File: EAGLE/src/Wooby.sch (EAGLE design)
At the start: 14 parts, among them J1 TB001-500-04BE, J2 TB001-500-04BE, J3 TB001-500-04BE, U1 GY-521MPU6050

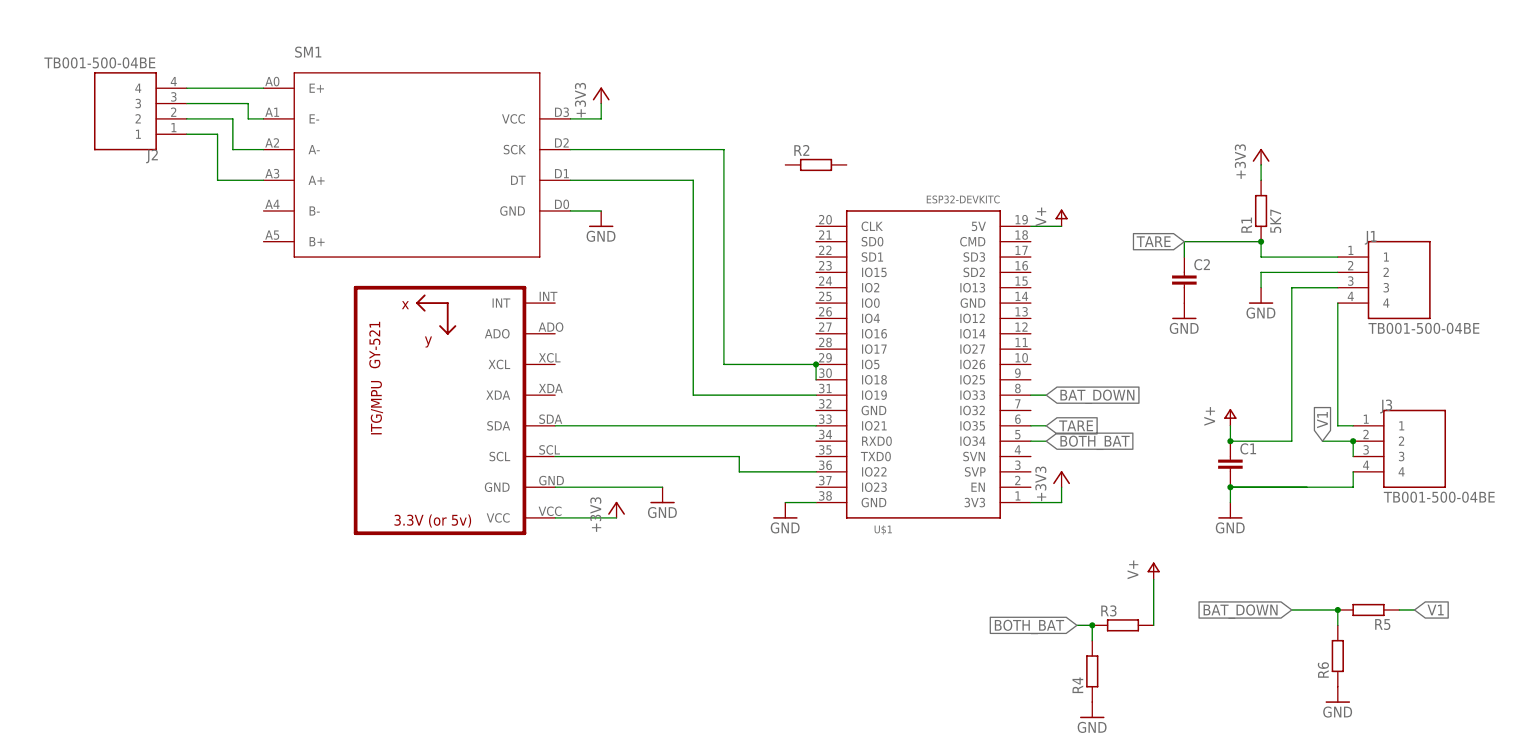
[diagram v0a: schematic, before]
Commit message: [PCB] Size 106mm x 40mm with terminal blocks 5mm, 2 pins.
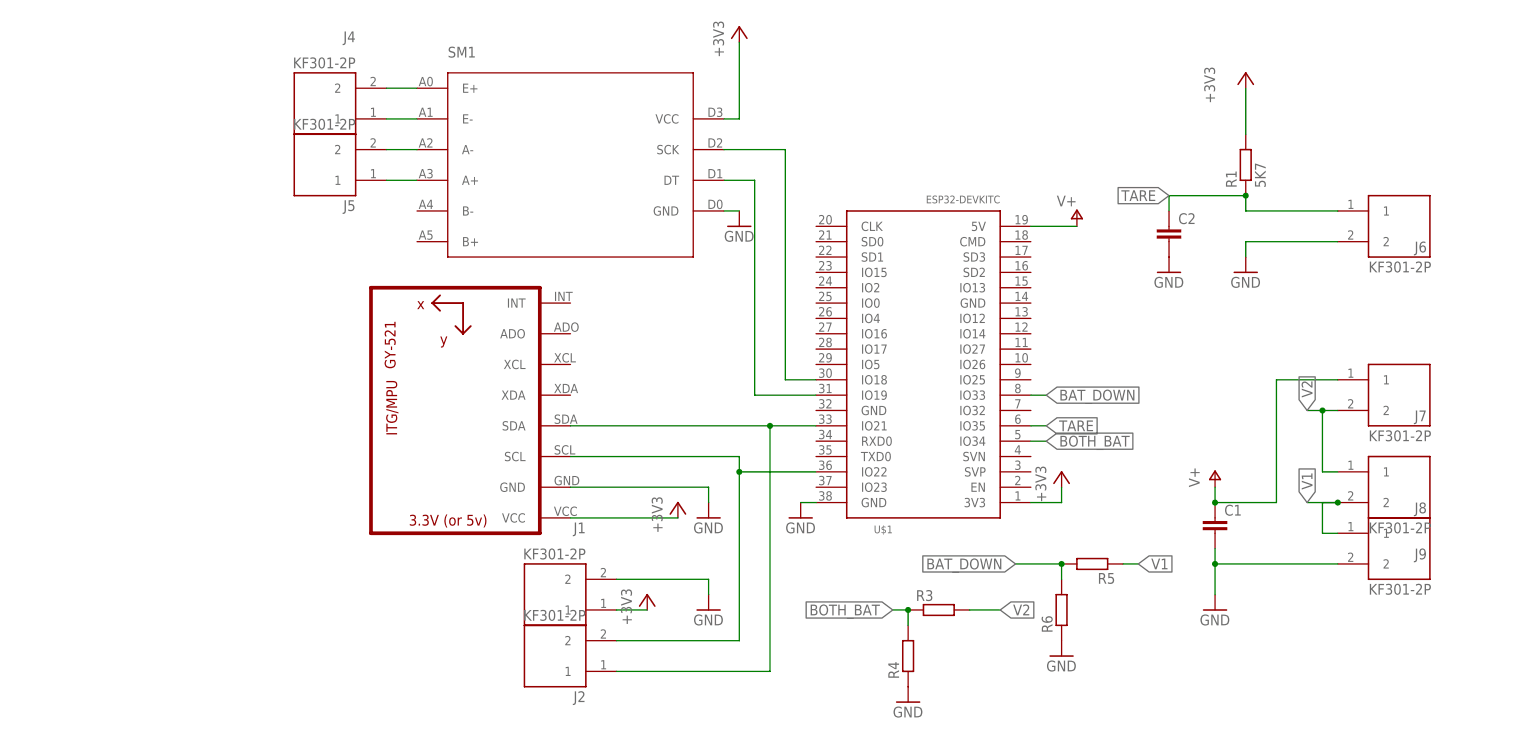
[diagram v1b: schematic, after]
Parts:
- removed J3: TB001-500-04BE, TB001-500-04BE:TB001-500-04BE
- removed R2: (no value), rcl:R-EU_0207/10
- added J4, J5, J6, J7, J8, J9: KF301-2P, KF301-2P:KF301-2P
- J1, J2: value TB001-500-04BE -> KF301-2P; device TB001-500-04BE:TB001-500-04BE -> KF301-2P:KF301-2P
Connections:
- removed net N$1: J1.4, J3.1
- new net V2: J7.2, J8.1, R3.2
- net +3V3: now also J1.1
- net GND: now also J6.2, J9.2; no longer J3.4
- net N$10: no longer U$1.IO5
- net N$2: now also J4.2; no longer J2.4
- net N$3: now also J4.1; no longer J2.3
- net N$4: now also J5.2; no longer J2.2
- net N$5: now also J5.1; no longer J2.1
- net N$6: now also J2.2
- net N$7: now also J2.1
- net TARE: now also J6.1; no longer J1.1
- net V+: now also J7.1; no longer J1.3, R3.2
- net V1: now also J8.2, J9.1; no longer J3.2, J3.3
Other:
- moved on the sheet: C1, C2, R1, R3, R4, R5, R6, SM1

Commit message: [PCB] Version 1
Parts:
- removed J1, J4, J6, J7, J8, J9: KF301-2P, KF301-2P:KF301-2P
- added BAT_BOT, BAT_TOP, CELL, LCD, ON_BTN, TARE: 691210910002, 691210910002:691210910002
- J2, J5: value KF301-2P -> 691210910002; device KF301-2P:KF301-2P -> 691210910002:691210910002
- renumbered U$1 to ESP32-DEVKITC
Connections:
- removed net N$3 (its old number): J4.1, SM1.E-
- new net N$1: CELL.1, SM1.E-
- net +3V3: now also LCD.1; no longer J1.1
- net BAT_DOWN: now also ESP32-DEVKITC.BAT_BOT; no longer ESP32-DEVKITC.IO33
- net BOTH_BAT: now also ESP32-DEVKITC.BATS; no longer ESP32-DEVKITC.IO34
- net GND: now also BAT_BOT.2, LCD.2, TARE.2; no longer J1.2, J6.2, J9.2
- net N$10: now also ESP32-DEVKITC.SCK; no longer ESP32-DEVKITC.IO18
- net N$2: now also CELL.2; no longer J4.2
- net N$6: now also ESP32-DEVKITC.SCL; no longer ESP32-DEVKITC.IO22
- net N$7: now also ESP32-DEVKITC.SDA; no longer ESP32-DEVKITC.IO21
- net TARE: now also ESP32-DEVKITC.TARE, TARE.1; no longer ESP32-DEVKITC.IO35, J6.1
- net V+: now also ON_BTN.1; no longer J7.1
- net V1: now also BAT_BOT.1, BAT_TOP.2; no longer J8.2, J9.1
- net V2: now also BAT_TOP.1, ON_BTN.2; no longer J7.2, J8.1

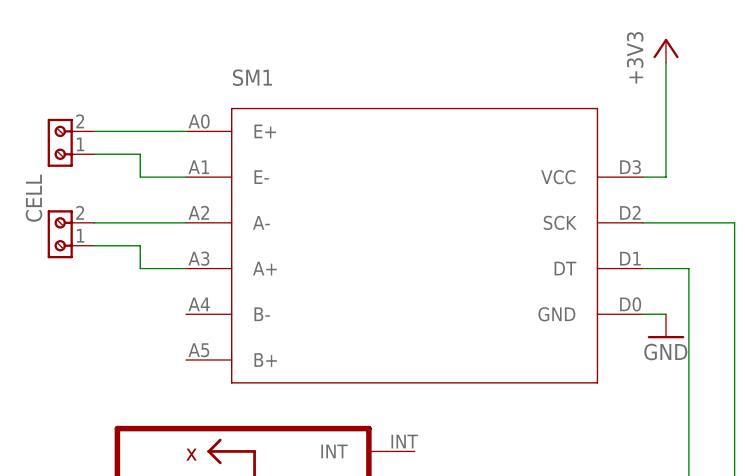
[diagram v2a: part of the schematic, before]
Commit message: Changes on several folders
EAGLE:
Small change to name the inputs of the HX711
ESP32:
Update with latest code with Bluetooth (not working). A cleaning will be done to make it work.
Python:
Latest code with the library and new datasets.
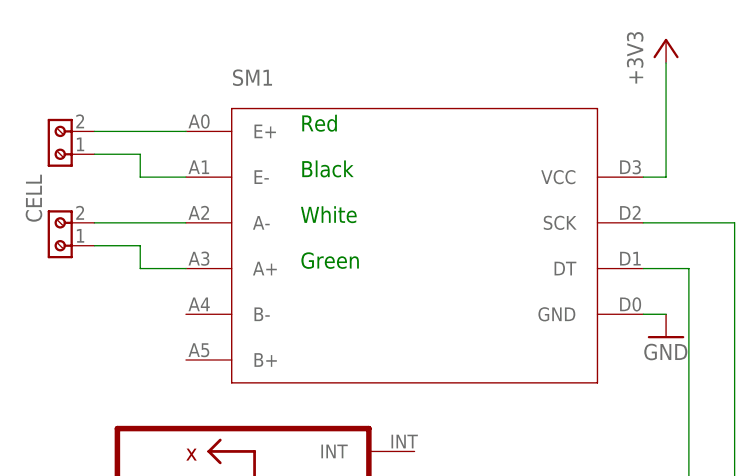
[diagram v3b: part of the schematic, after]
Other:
- note added: "Black"
- note added: "Green"
- note added: "Red"
- note added: "White"
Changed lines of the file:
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@@
 <?xml version="1.0" encoding="utf-8"?>
 <!DOCTYPE eagle SYSTEM "eagle.dtd">
-<eagle version="9.6.1">
+<eagle version="9.6.2">
 <drawing>
 <settings>
@@
 <sheet>
 <plain>
+<text x="2.54" y="68.58" size="1.778" layer="91">Green</text>
+<text x="2.54" y="78.74" size="1.778" layer="91">Black</text>
+<text x="2.54" y="73.66" size="1.778" layer="91">White</text>
+<text x="2.54" y="83.82" size="1.778" layer="91">Red</text>
 </plain>
 <instances>

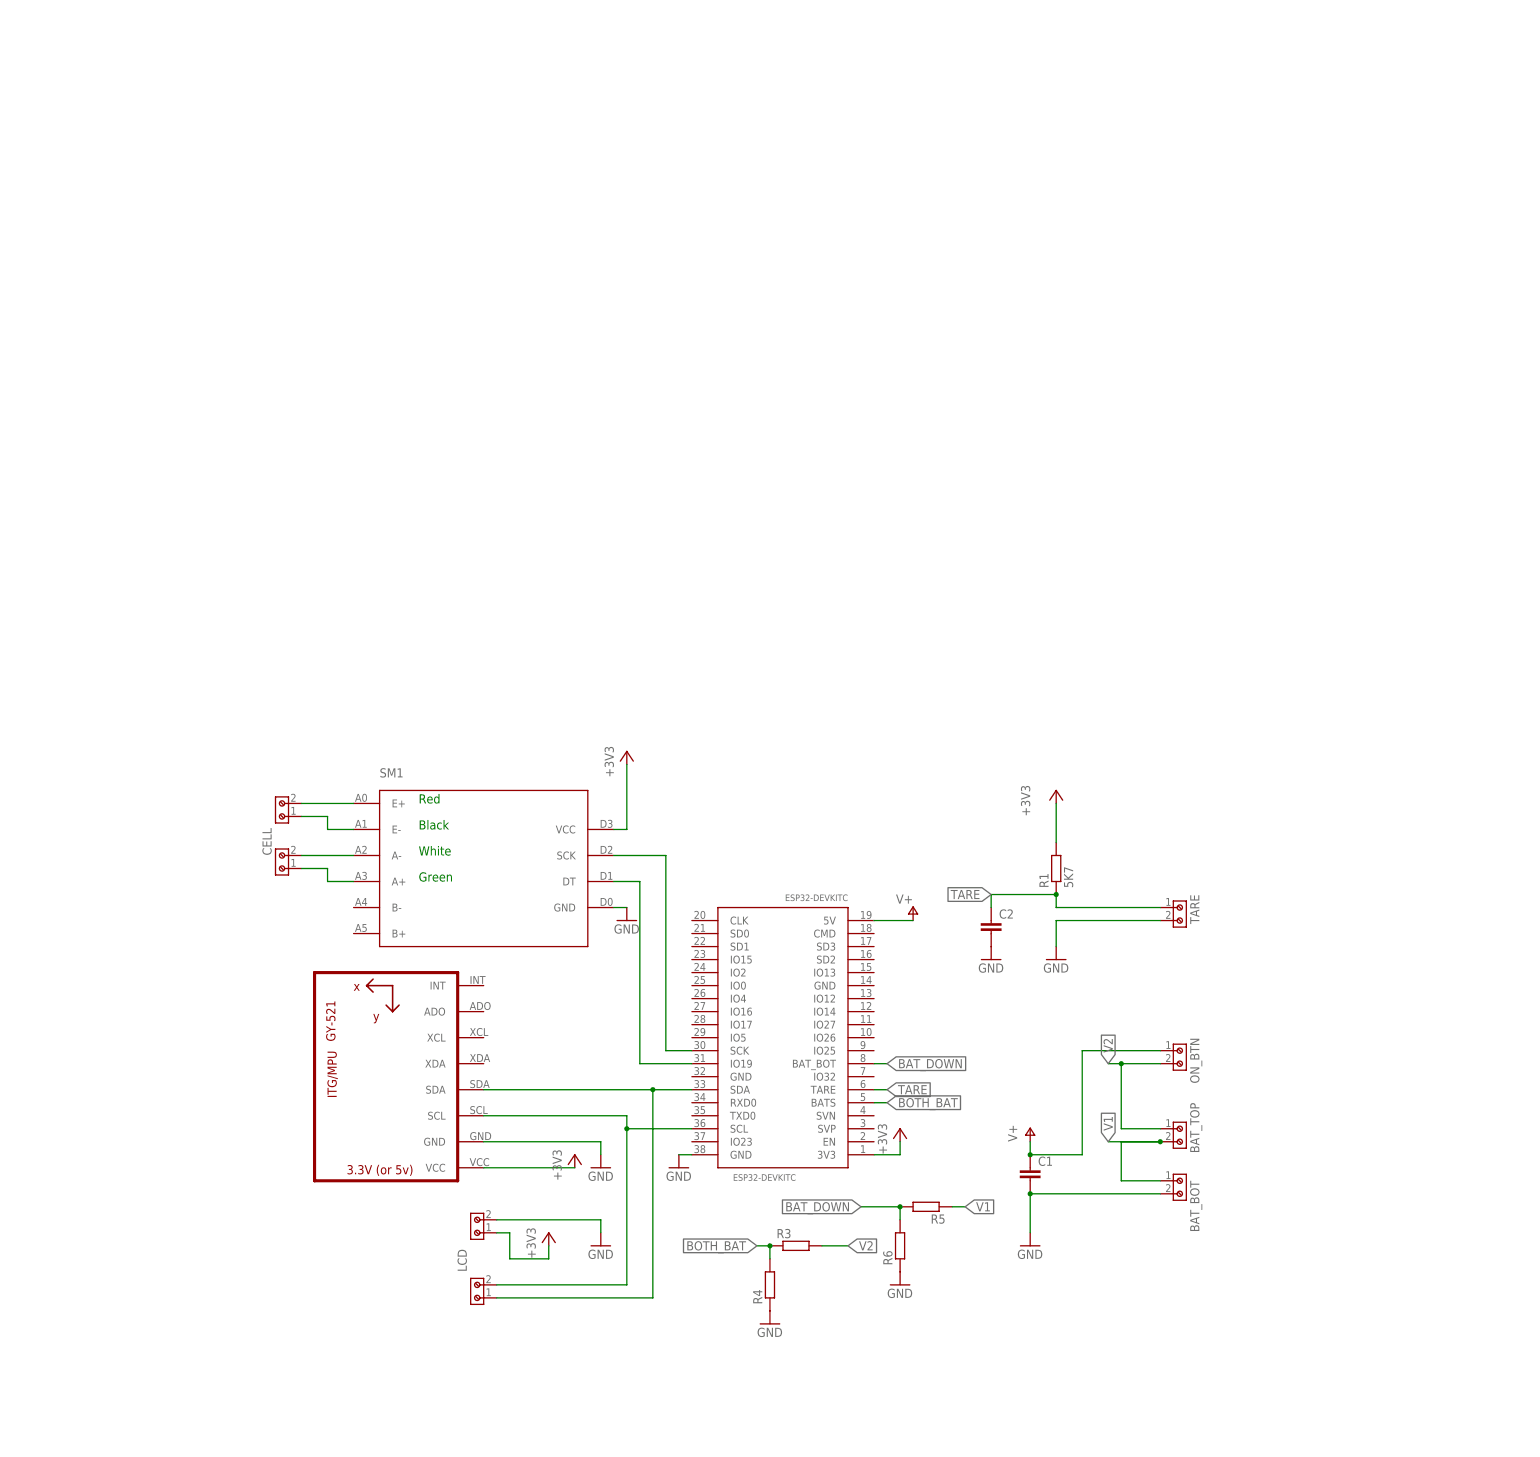
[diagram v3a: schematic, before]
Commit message: EagleV2
With some improvements since the first V" printed version, but still with some improvements to be performed
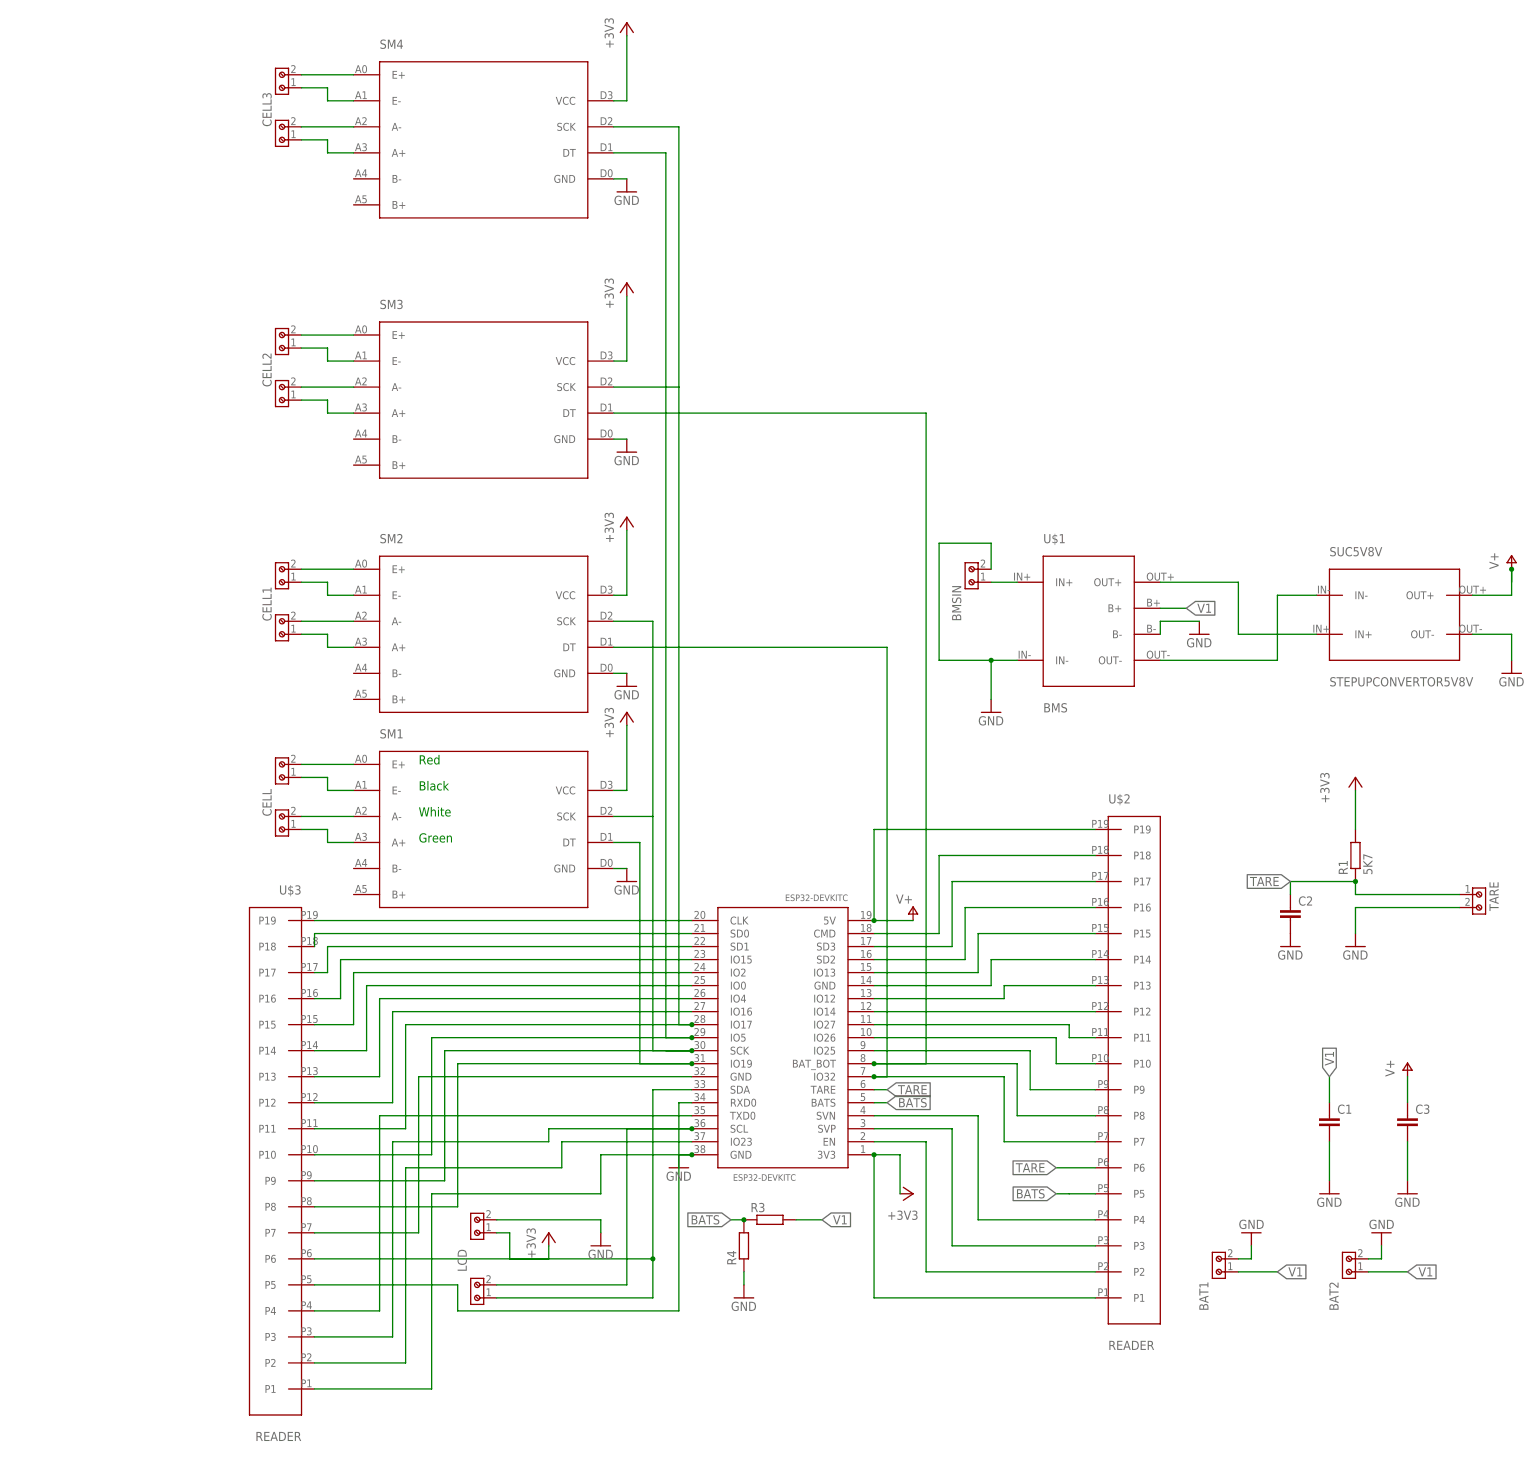
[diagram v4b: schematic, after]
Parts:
- removed BAT_BOT, BAT_TOP, ON_BTN: 691210910002, 691210910002:691210910002
- removed R5, R6: (no value), rcl:R-EU_0207/10
- removed U1: GY-521MPU6050, MPU-6050:GY-521MPU6050
- added BAT1, BAT2, BMSIN, CELL1, CELL2, CELL3, J1, J3, J4: 691210910002, 691210910002:691210910002
- added C3: (no value), capacitor-wima:C5/3
- added SM2, SM3, SM4: (no value), hx711:HX711
- added SUC5V8V: STEPUPCONVERTOR5V8V, stepUpConverto5V8V:STEPUPCONVERTOR5V8V
- added U$1: BMS, BMS:BMS
- added U$2, U$3: READER, READER:READER
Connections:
- removed net BAT_DOWN: ESP32-DEVKITC.BAT_BOT, R5.2, R6.2
- removed net BOTH_BAT: ESP32-DEVKITC.BATS, R3.1, R4.2
- removed net V2: BAT_TOP.1, ON_BTN.2, R3.2
- new net BATS: ESP32-DEVKITC.BATS, R3.1, R4.2, U$2.P5
- new net N$11: ESP32-DEVKITC.BAT_BOT, SM3.DT, U$2.P8
- new net N$12: ESP32-DEVKITC.IO5, SM4.DT, U$3.P10
- new net N$13: CELL3.2, SM4.E+
- new net N$14: CELL3.1, SM4.E-
- new net N$15: J4.2, SM4.A-
- new net N$16: J4.1, SM4.A+
- new net N$17: CELL2.2, SM3.E+
- new net N$18: CELL2.1, SM3.E-
- new net N$19: J3.2, SM3.A-
- new net N$20: J3.1, SM3.A+
- new net N$21: CELL1.2, SM2.E+
- new net N$22: CELL1.1, SM2.E-
- new net N$23: J1.2, SM2.A-
- new net N$24: J1.1, SM2.A+
- new net N$25: SUC5V8V.IN-, U$1.OUT-
- new net N$26: SUC5V8V.IN+, U$1.OUT+
- new net N$27: BMSIN.1, U$1.IN+
- new net N$28: ESP32-DEVKITC.CMD, U$2.P18
- new net N$29: ESP32-DEVKITC.SD3, U$2.P17
- new net N$30: ESP32-DEVKITC.SD2, U$2.P16
- new net N$31: ESP32-DEVKITC.IO13, U$2.P15
- new net N$32: ESP32-DEVKITC.GND@14, U$2.P14
- new net N$33: ESP32-DEVKITC.IO12, U$2.P13
- new net N$34: ESP32-DEVKITC.IO14, U$2.P12
- new net N$35: ESP32-DEVKITC.IO27, U$2.P11
- new net N$36: ESP32-DEVKITC.IO26, U$2.P10
- new net N$37: ESP32-DEVKITC.IO25, U$2.P9
- new net N$38: ESP32-DEVKITC.SVN, U$2.P4
- new net N$39: ESP32-DEVKITC.SVP, U$2.P3
- new net N$40: ESP32-DEVKITC.EN, U$2.P2
- new net N$41: ESP32-DEVKITC.CLK, U$3.P19
- new net N$42: ESP32-DEVKITC.SD0, U$3.P18
- new net N$43: ESP32-DEVKITC.SD1, U$3.P17
- new net N$44: ESP32-DEVKITC.IO15, U$3.P16
- new net N$45: ESP32-DEVKITC.IO2, U$3.P15
- new net N$46: ESP32-DEVKITC.IO0, U$3.P14
- new net N$47: ESP32-DEVKITC.IO4, U$3.P13
- new net N$48: ESP32-DEVKITC.IO16, U$3.P12
- new net N$49: ESP32-DEVKITC.GND@32, U$3.P7
- new net N$5: ESP32-DEVKITC.IO32, SM2.DT, U$2.P7
- new net N$50: ESP32-DEVKITC.RXD0, U$3.P5
- new net N$51: ESP32-DEVKITC.TXD0, U$3.P4
- new net N$53: ESP32-DEVKITC.IO23, U$3.P2
- new net N$8: ESP32-DEVKITC.IO17, SM3.SCK, SM4.SCK, U$3.P11
- net +3V3: now also SM2.VCC, SM3.VCC, SM4.VCC, U$2.P1; no longer U1.VCC
- net GND: now also BAT1.2, BAT2.2, BMSIN.2, C3.2, SM2.GND, SM3.GND, SM4.GND, SUC5V8V.OUT-, U$1.B-, U$1.IN-, U$3.P1; no longer BAT_BOT.2, R6.1, U1.GND
- net N$10: now also SM2.SCK, U$3.P9
- net N$6: now also U$3.P3; no longer U1.SCL
- net N$7: now also U$3.P6; no longer U1.SDA
- net N$9: now also U$3.P8
- net TARE: now also U$2.P6
- net V+: now also C3.1, SUC5V8V.OUT+, U$2.P19; no longer C1.1, ON_BTN.1
- net V1: now also BAT1.1, BAT2.1, C1.1, R3.2, U$1.B+; no longer BAT_BOT.1, BAT_TOP.2, R5.1
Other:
- moved on the sheet: C1, C2, CELL, R1, R3, R4, SM1, TARE
